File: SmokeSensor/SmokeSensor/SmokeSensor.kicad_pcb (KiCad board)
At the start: 2 copper layers, 84 x 63 mm, 59 parts, among them J1 USB_C_Receptacle_USB2.0_16P, J2 Conn_01x05_Pin, J3 Conn_01x11, J4 Conn_01x04, J5 Pin lithium, J6 Switch, Q1 SS8050, Q2 SS8050, SW1 RESET, SW2 BOOT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

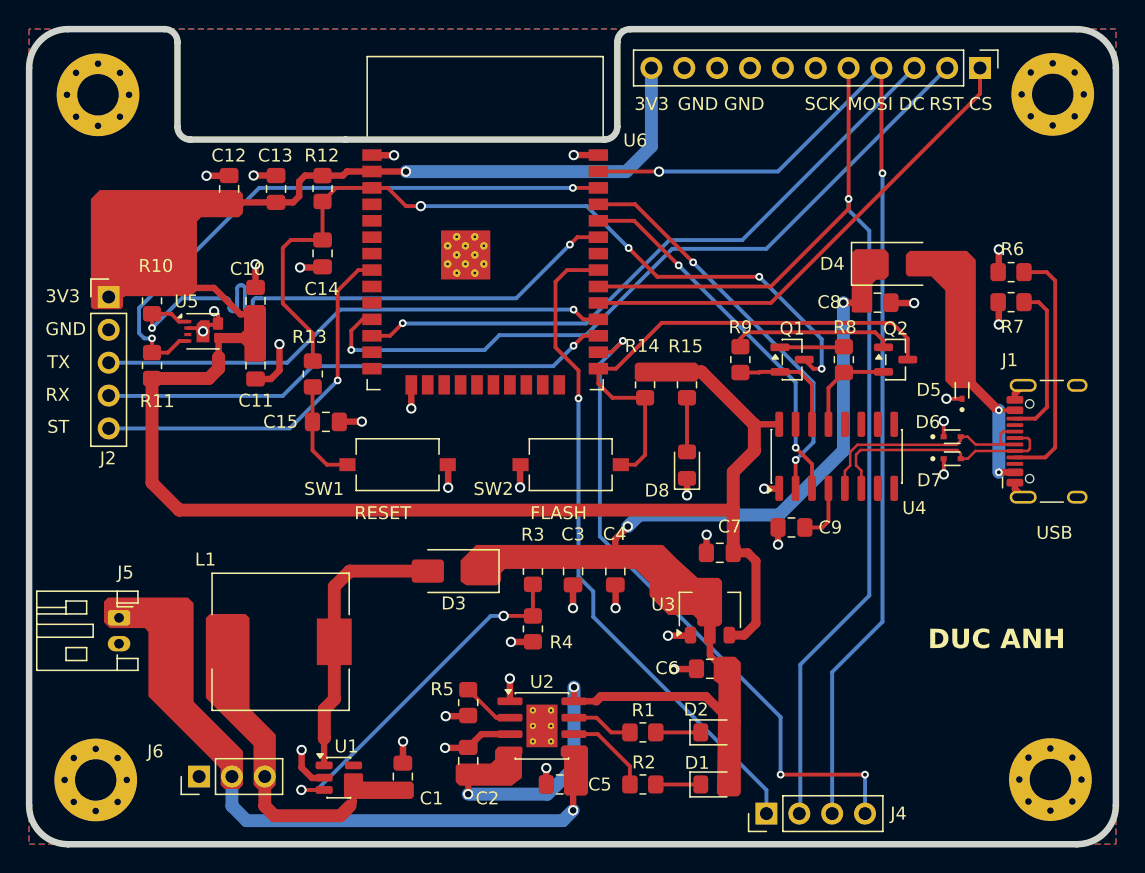
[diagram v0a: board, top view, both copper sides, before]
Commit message: add vias Gnd
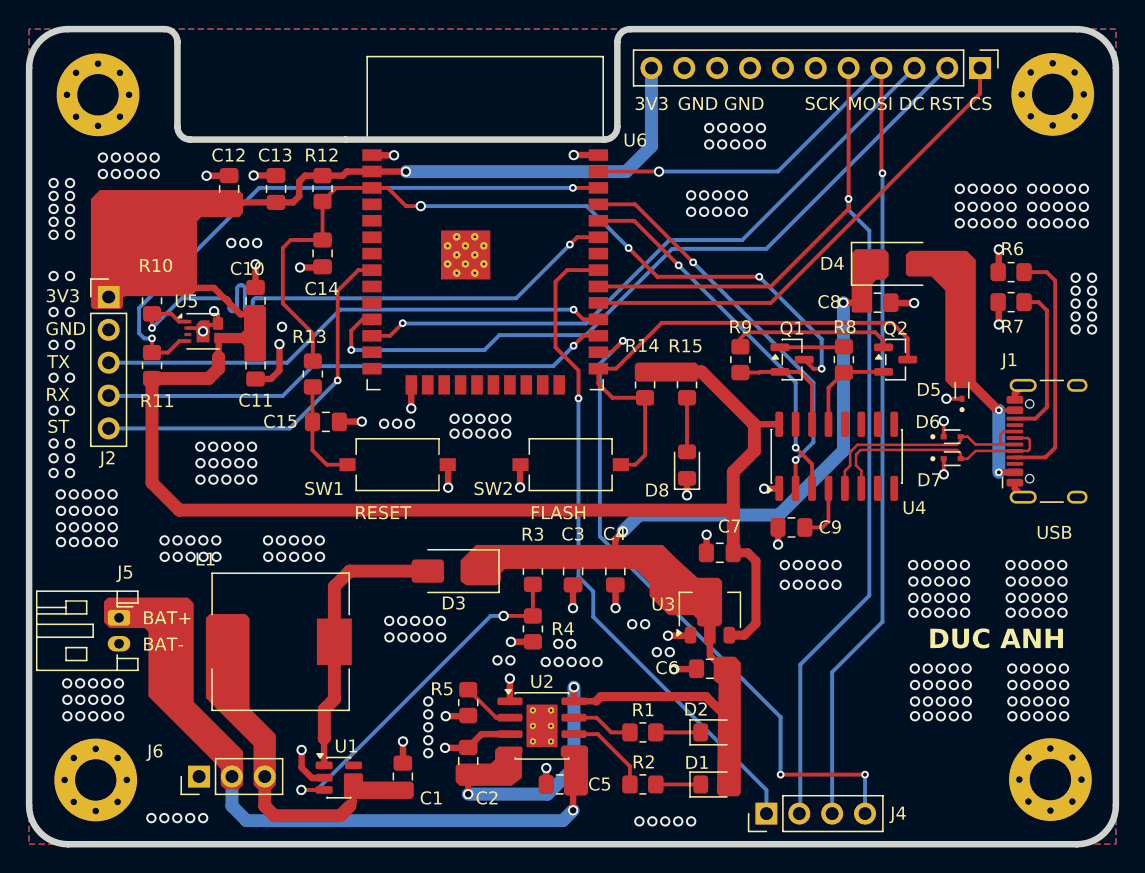
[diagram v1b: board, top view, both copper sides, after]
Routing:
- net GND: vias 34 -> 345
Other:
- board text added: "BAT+"
- board text added: "BAT-"
